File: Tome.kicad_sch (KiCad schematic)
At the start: 121 parts, among them J1 USB_C_Receptacle_USB2.0_14P, J2 [battery connector], J3 SD_Card_Receptacle, J4 [bootstrap jumper], J5 AudioJack3, J6 Conn_01x24_Socket, J7 Conn_01x24_Socket, Q1 DMG3415, Q2 DMG3415, Q3 Si1308EDL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

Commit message: split schematic based on physical PCB split
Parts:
- removed C1, C2, C3: 10u, symbol Device:C_Small
- removed C10, C11, C12, C13, C14, C15, C4, C5, C7, C9: 100n, symbol Device:C_Small
- removed C16, C17: 15p, symbol Device:C_Small
- removed C18, C19, C20, C21, C22, C23, C24, C25, C26, C6, C8: 1u, symbol Device:C_Small
- removed C27, C28, C31: 2.2u, symbol Device:C_Small
- removed C29, C30: 2.2n, symbol Device:C_Small
- removed C32, C33, C36, C39: 0.1u, symbol Device:C_Small
- removed C34, C35, C37, C38: 10u, symbol Device:C_Polarized_Small
- removed C40, C43, C44, C47, C49, C50, C52, C53, C54, C55, C56, C57, C58, C59: 4.7uF, symbol Device:C_Small
- removed C41, C42, C45, C46, C48, C51: 1uF, symbol Device:C_Small
- removed D1, D2, D3, D5, D6, D7: MBR0530, Diode_SMD:D_SOD-123, symbol Diode:MBR0530
- removed D4: MBR120, Diode_SMD:D_SOD-123, symbol Device:D_Schottky
- removed J1: USB_C_Receptacle_USB2.0_14P, symbol Connector:USB_C_Receptacle_USB2.0_14P
- removed J2: [battery connector], symbol Connector:Conn_01x02_Socket
- removed J3: SD_Card_Receptacle, symbol Connector:SD_Card_Receptacle
- removed J4: [bootstrap jumper], symbol Connector:Conn_01x02_Pin
- removed J5: AudioJack3, symbol Connector_Audio:AudioJack3
- removed J6, J7: Conn_01x24_Socket, symbol Connector:Conn_01x24_Socket
- removed L1, L2: 47uH, symbol Device:L_Small
- removed Q1, Q2: DMG3415, Package_TO_SOT_SMD:SOT-23, symbol Device:Q_PMOS_GSD
- removed Q3, Q4: Si1308EDL, Package_TO_SOT_SMD:SOT-323_SC-70, symbol Transistor_FET:Si1308EDL
- removed R1, R2: 5.1k, symbol Device:R_Small
- removed R10, R3, R9: 1k, symbol Device:R_Small
- removed R11, R16, R17, R18, R22, R29, R30, R31, R33, R34, R7, R8: 10k, symbol Device:R_Small
- removed R12, R13, R14, R4: 100k, symbol Device:R_Small
- removed R15: 200k, symbol Device:R_Small
- removed R19, R20: 470, symbol Device:R_Small
- removed R21, R25: 2.2, symbol Device:R_Small
- removed R23, R24: 1M, symbol Device:R_Small
- removed R5, R6: 27.4, symbol Device:R_Small
- removed SW1: [reset button], symbol Switch:SW_Push
- removed SW2, SW3, SW5: SW_SPST, symbol Switch:SW_SPST
- removed U1: RP2040, Package_DFN_QFN:QFN-56-1EP_7x7mm_P0.4mm_EP3.2x3.2mm, symbol MCU_RaspberryPi:RP2040
- removed U2: XC6220B331MR, Package_TO_SOT_SMD:SOT-23-5, symbol Regulator_Linear:XC6220B331MR
- removed U3: MCP73831-2-OT, Package_TO_SOT_SMD:SOT-23-5, symbol Battery_Management:MCP73831-2-OT
- removed U4: W25Q128JVS, Package_SO:SOIC-8_5.3x5.3mm_P1.27mm, symbol Memory_Flash:W25Q128JVS
- removed U5: TLV70033_SOT23-5, Package_TO_SOT_SMD:SOT-23-5, symbol Regulator_Linear:TLV70033_SOT23-5
- removed U6: PCM5102APW, PCM5102A:PW0020A_L, symbol PCM5102A:PCM5102APW
- removed U7: PAM8908, Package_DFN_QFN:QFN-16-1EP_3x3mm_P0.5mm_EP1.7x1.7mm, symbol Amplifier_Audio:PAM8908
- removed Y1: ABM8-272-T3, symbol Device:Crystal_GND24
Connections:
- no-connect marks 14 -> 0
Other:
- removed sheet encoder_daughter_1
- removed sheet encoder_daughter_2
- added sheet control_side (control_mainboard.kicad_sch)
- added sheet peripheral_side (peripheral_mainboard.kicad_sch)
- note removed: "(+4V)"
- note removed: "6dB gain by default throw SW2 for 0dB gain"
- note removed: "ANALOG POWER"
- note removed: "AUDIO OUT (DAC + AMP + JACK)"
- note removed: "BATTERY + MONITOR"
- note removed: "C6 should be close to RP2040 pin 45"
- note removed: "C8 should be close to RP2040 pin 44"
- note removed: "CONTROL KNOBS"
- note removed: "DISPLAY CONNECTORS + POWER"
- note removed: "PERIPHERAL POWER CONTROL"
- note removed: "RP2040 + FLASH + CRYSTAL"
- note removed: "SD CARD SLOT"
- note removed: "USB + POWER"
- note removed: "max current draw 200mA"
- note removed: "mute switch"
- note removed: "placing jumper between pins of J4 and reseting will put RP2040 into BOOTSEL mode instead of running contents of flash storage"
- note removed: "polarized capacitors are electrolytic capacitors"

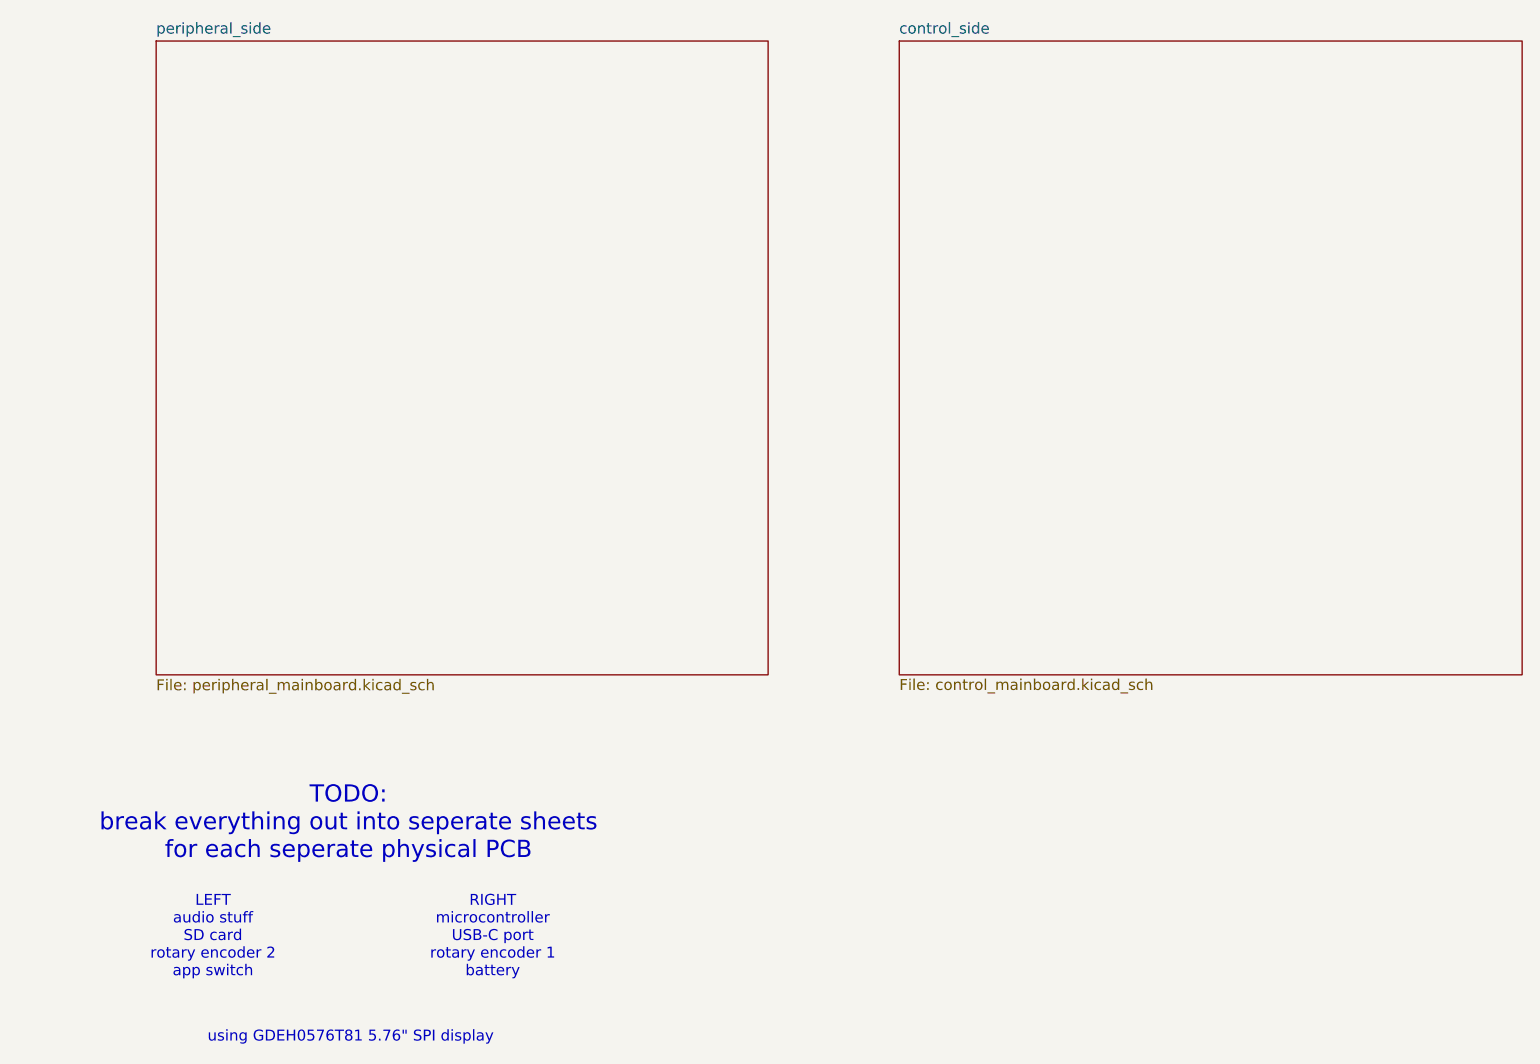
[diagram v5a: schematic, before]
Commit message: separating schematics based on board
finished splitting every component up into separate sheets in the schematic based on what physical board it's going on
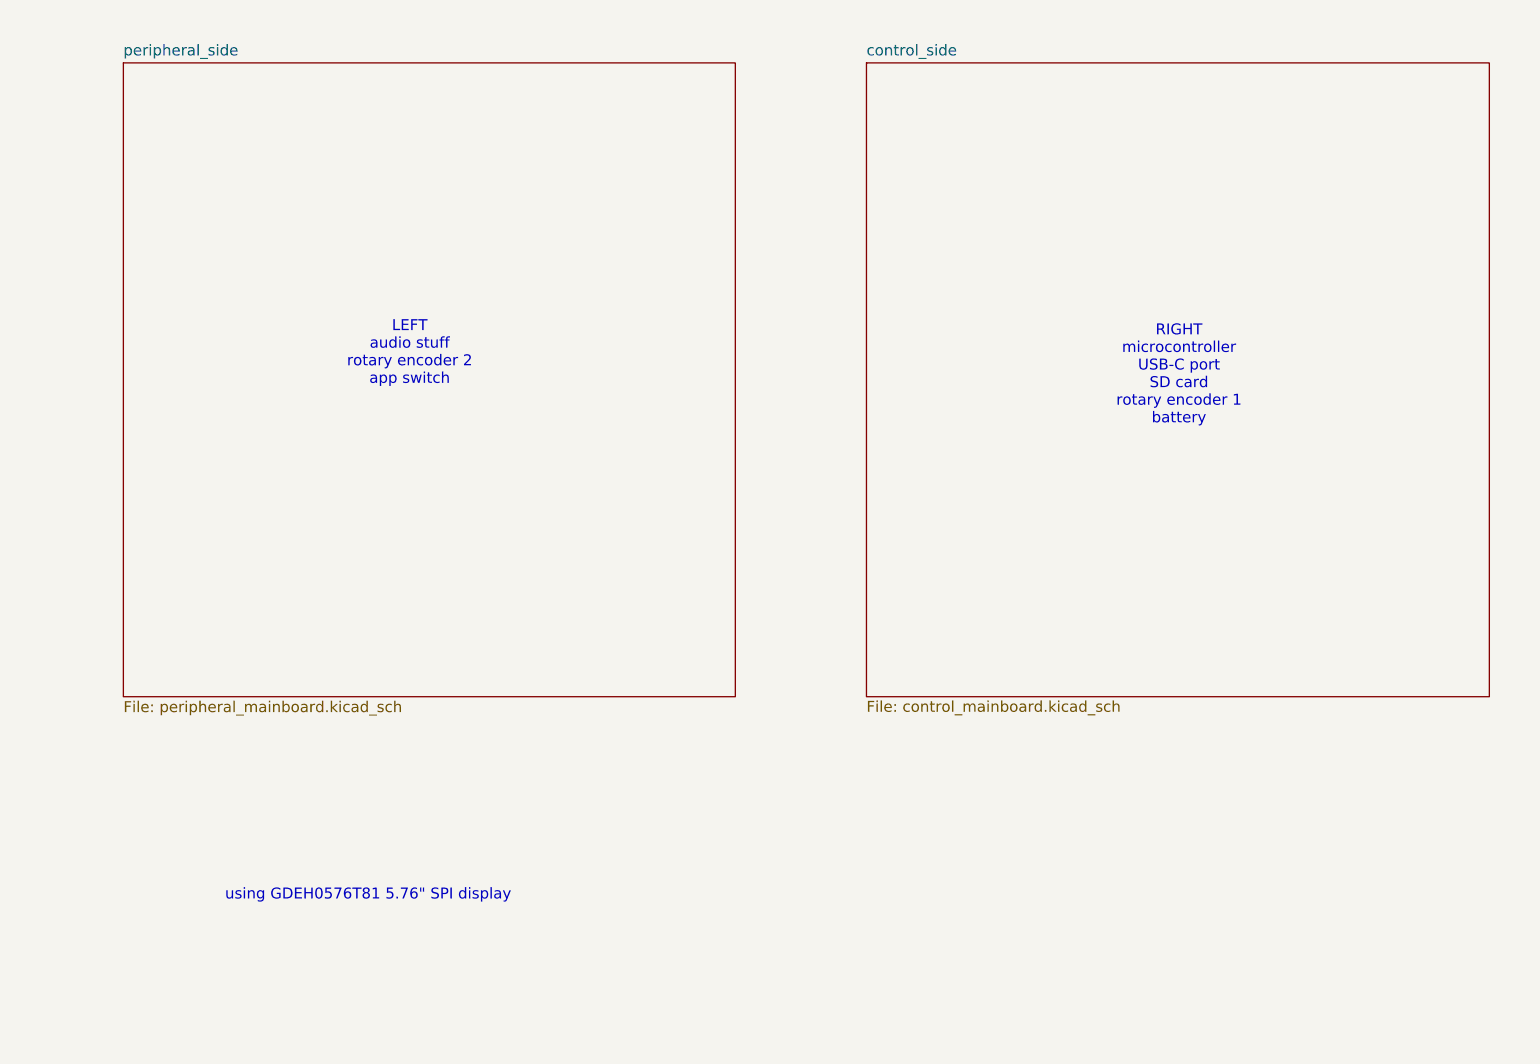
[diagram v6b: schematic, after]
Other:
- note added: "LEFT audio stuff rotary encoder 2 app switch"
- note added: "RIGHT microcontroller USB-C port SD card rotary encoder 1 battery"
- note removed: "LEFT audio stuff SD card rotary encoder 2 app switch"
- note removed: "RIGHT microcontroller USB-C port rotary encoder 1 battery"
- note removed: "TODO: break everything out into seperate sheets for each seperate physical PCB"
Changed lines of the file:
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@@
 		(company "rien+la_reine;")
 	)
-	(text "TODO:\nbreak everything out into seperate sheets\nfor each seperate physical PCB"
+	(text "RIGHT\nmicrocontroller\nUSB-C port\nSD card\nrotary encoder 1\nbattery"
 		(exclude_from_sim no)
-		(at 50.292 109.982 0)
-		(effects
-			(font
-				(size 2 2)
-			)
-		)
-	)
-	(text "RIGHT\nmicrocontroller\nUSB-C port\nrotary encoder 1\nbattery"
-		(exclude_from_sim no)
-		(at 67.056 123.19 0)
+		(at 146.812 57.912 0)
 		(effects
 			(font
@@
 		)
 	)
-	(text "LEFT\naudio stuff\nSD card\nrotary encoder 2\napp switch"
+	(text "LEFT\naudio stuff\nrotary encoder 2\napp switch"
 		(exclude_from_sim no)
-		(at 34.544 123.19 0)
+		(at 57.404 55.372 0)
 		(effects
 			(font
@@
 	(text "using GDEH0576T81 5.76\" SPI display"
 		(exclude_from_sim no)
-		(at 50.546 134.874 0)
+		(at 52.578 118.364 0)
 		(effects
 			(font
@@
 	)
 	(sheet
-		(at 27.94 19.05)
+		(at 24.13 21.59)
 		(size 71.12 73.66)
 		(exclude_from_sim no)
@@
 		)
 		(property "Sheetname" "peripheral_side"
-			(at 27.94 18.3384 0)
+			(at 24.13 20.8784 0)
 			(effects
 				(font
@@
 		)
 		(property "Sheetfile" "peripheral_mainboard.kicad_sch"
-			(at 27.94 93.1686 0)
+			(at 24.13 95.7086 0)
 			(effects
 				(font
@@
 	)
 	(sheet
-		(at 114.3 19.05)
+		(at 110.49 21.59)
 		(size 72.39 73.66)
 		(exclude_from_sim no)
@@
 		)
 		(property "Sheetname" "control_side"
-			(at 114.3 18.3384 0)
+			(at 110.49 20.8784 0)
 			(effects
 				(font
@@
 		)
 		(property "Sheetfile" "control_mainboard.kicad_sch"
-			(at 114.3 93.1346 0)
+			(at 110.49 95.6746 0)
 			(effects
 				(font

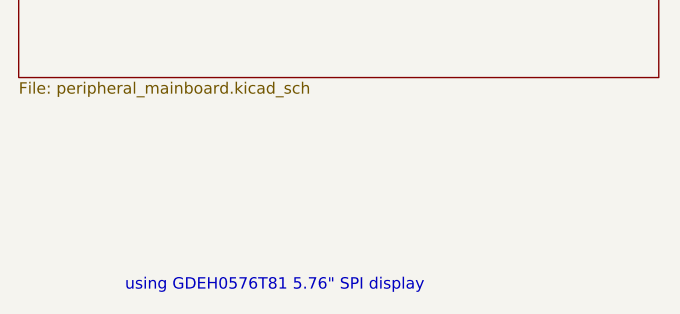
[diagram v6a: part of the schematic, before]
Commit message: finalizing schematics
connected the new DAC footprint, filled in title blocks
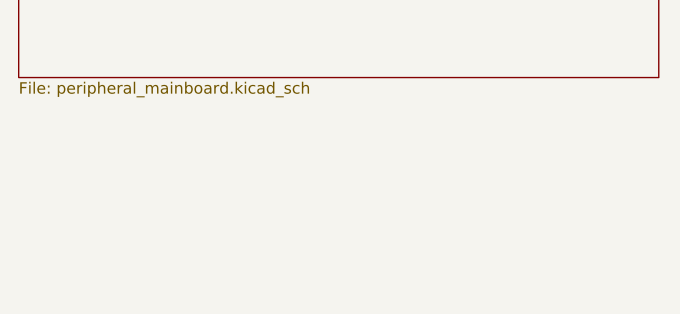
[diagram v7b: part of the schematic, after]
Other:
- note removed: "using GDEH0576T81 5.76" SPI display"
